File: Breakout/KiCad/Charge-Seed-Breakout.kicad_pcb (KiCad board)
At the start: 4 copper layers, 125 x 101 mm, 16 parts, among them U1 JL308-25410G01, U10 JL308-25410G01, U2 JL308-25410G01, U3 P125-1120A0BS116A1, U4 2541FV-20P-B, U5 2541FV-20P-B, U6 P125-1120A0BS116A1, U7 2541FV-20P-B, U8 2541FV-20P-B, U9 JL308-25410G01

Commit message: Exported as v0.1 for production.
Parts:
- removed H1, H2, H3, H4, H5, H6: MountingHole_Pad, clectric-diy:MountingHole_AE
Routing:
- added copper zone on B.Cu, net (none)
- added copper zone on F.Cu, net (none)
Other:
- board text added: "Copyright © 2025 clectric.diy Licensed under CERN-OHL-S v2"
- board text added: "clectric.diy Charge Seed Breakout Board"

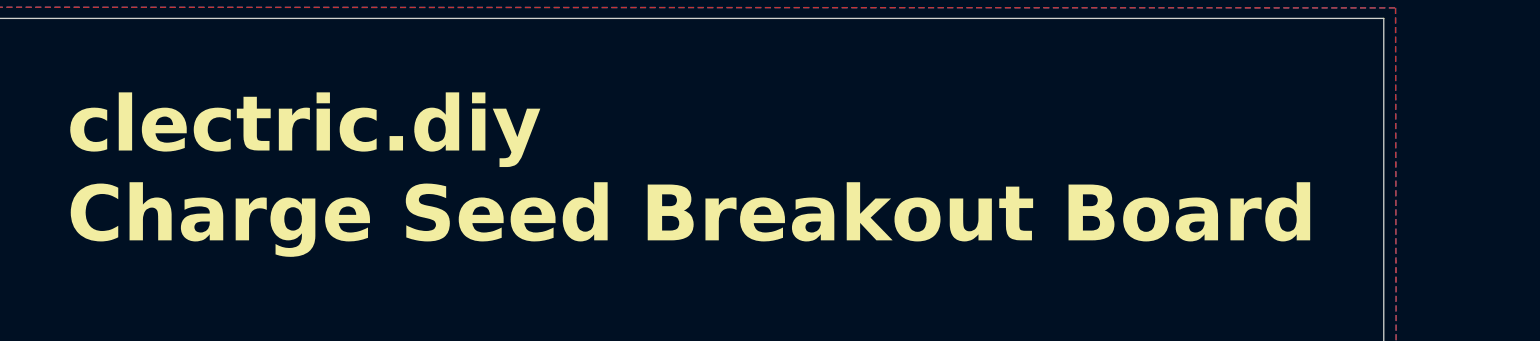
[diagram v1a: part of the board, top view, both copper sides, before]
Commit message: Updated board's title in silkscreen to be correct.
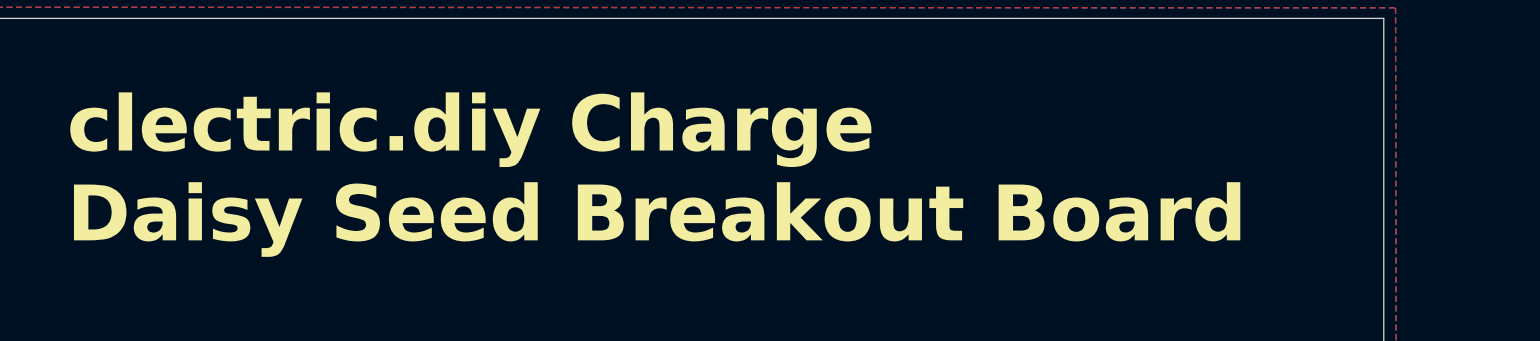
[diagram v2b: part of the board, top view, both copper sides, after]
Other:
- board text added: "clectric.diy Charge Daisy Seed Breakout Board"
- board text removed: "clectric.diy Charge Seed Breakout Board"
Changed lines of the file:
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@@
 		)
 	)
-	(gr_text "clectric.diy\nCharge Seed Breakout Board"
+	(gr_text "clectric.diy Charge\nDaisy Seed Breakout Board"
 		(at 63.894637 58.507679 0)
 		(layer "F.SilkS")
